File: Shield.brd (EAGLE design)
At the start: 53.3 x 55.9 mm, 26 parts, among them J1 AVR_SPI_PRG_6PTH, Q8 TIP120, U2 LM78XX-TO252-3, U4 ATMEGA328P_PDIP, Y1 16Mhz

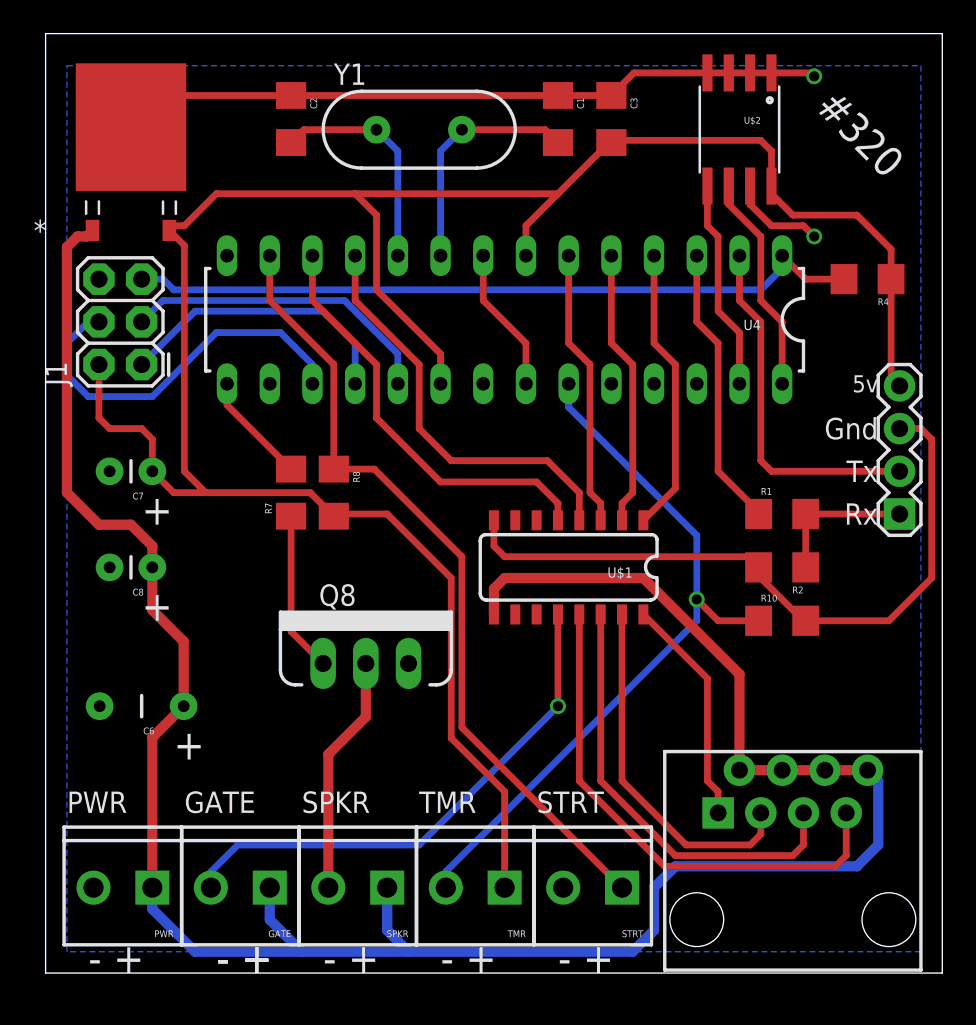
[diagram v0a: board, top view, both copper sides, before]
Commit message: Fixed 12v relay voltage
git-svn-id: svn+ssh://petrocik.net/home/svn/repo/uci_gate/branches/hardware/uci_gate/3.x@133 8c868176-b666-4d83-8e7f-acb7c29fc81a
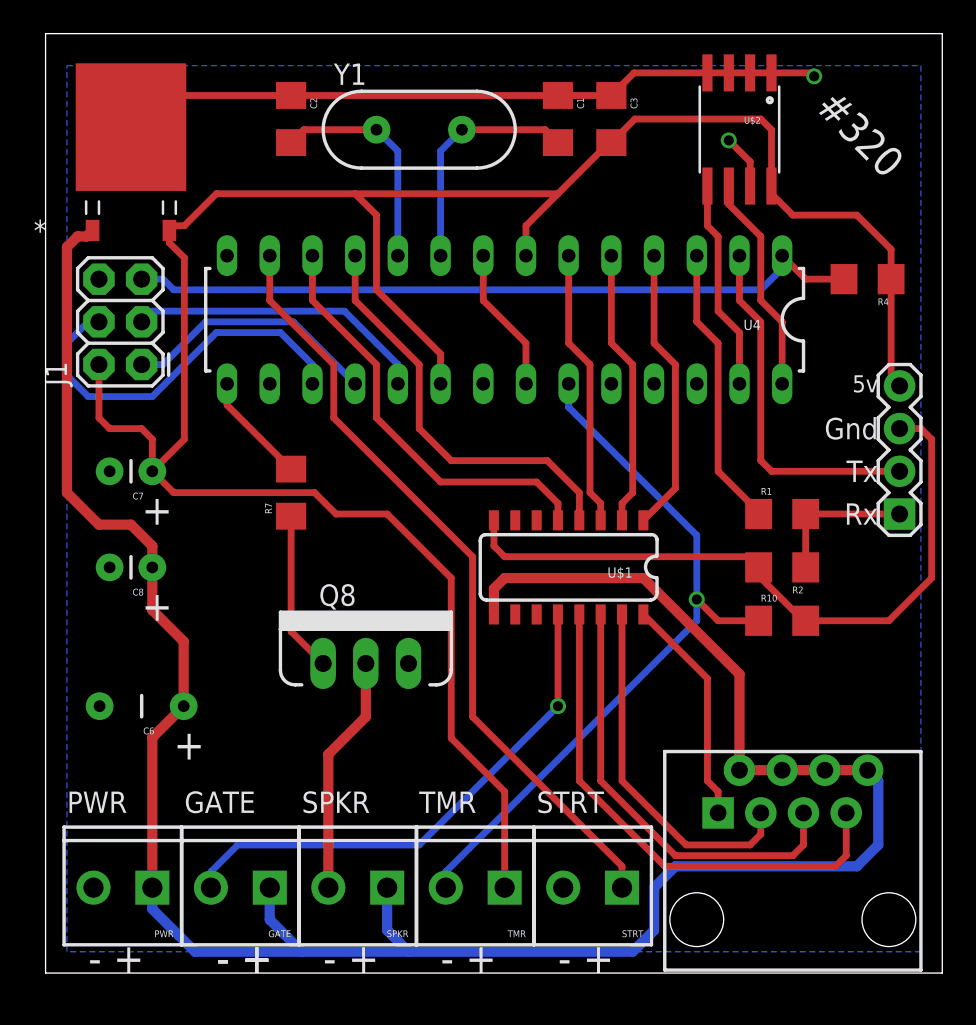
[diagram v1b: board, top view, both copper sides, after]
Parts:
- removed R8: 10K, SparkFun-Passives:1206
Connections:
- net 5V: no longer R8.2
- net D7: no longer R8.1
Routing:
- net GND: track 98.7 -> 96.3 mm
- net MISO: track 17.2 -> 15.3 mm
- net D7: track 47.7 -> 46.3 mm
- net SCK: track 18.9 -> 18.0 mm
- net 5V: track 141.1 -> 141.7 mm
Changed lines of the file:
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@@
 <?xml version="1.0" encoding="utf-8"?>
 <!DOCTYPE eagle SYSTEM "eagle.dtd">
-<eagle version="6.5.0">
+<eagle version="7.2.0">
 <drawing>
 <settings>
@@
 <pass name="Default">
 <param name="RoutingGrid" value="10mil"/>
+<param name="AutoGrid" value="1"/>
+<param name="Efforts" value="0"/>
+<param name="TopRouterVariant" value="1"/>
 <param name="tpViaShape" value="round"/>
 <param name="PrefDir.1" value="|"/>
@@
 <element name="SPKR" library="SparkFun-Connectors" package="SCREWTERMINAL-3.5MM-2" value="" x="20.32" y="5.08" rot="R180"/>
 <element name="Q8" library="ucigate" package="TO220V" value="TIP120" x="19.05" y="18.415"/>
-<element name="R8" library="SparkFun-Passives" package="1206" value="10K" x="17.145" y="28.575" rot="R270"/>
 <element name="STRT" library="SparkFun-Connectors" package="SCREWTERMINAL-3.5MM-2" value="" x="34.29" y="5.08" rot="R180"/>
 <element name="R10" library="SparkFun-Passives" package="1206" value="10K" x="43.815" y="20.955"/>
@@
 <wire x1="26.035" y1="40.005" x2="28.575" y2="37.465" width="0.4064" layer="1"/>
 <wire x1="28.575" y1="37.465" x2="28.575" y2="35.052" width="0.4064" layer="1"/>
-<polygon width="0.4064" layer="16">
+<polygon width="0.4064" layer="16" isolate="0.254">
 <vertex x="1.27" y="53.975"/>
 <vertex x="52.07" y="53.975"/>
@@
 <wire x1="50.8" y1="32.766" x2="50.8" y2="32.385" width="0.381" layer="1"/>
 <wire x1="43.18" y1="53.34" x2="43.18" y2="53.5432" width="0.381" layer="1"/>
-<via x="45.72" y="43.815" extent="1-16" drill="0.6"/>
-<wire x1="41.91" y1="46.8122" x2="41.91" y2="45.72" width="0.4064" layer="1"/>
-<wire x1="41.91" y1="45.72" x2="43.18" y2="44.45" width="0.4064" layer="1"/>
-<wire x1="43.18" y1="44.45" x2="45.085" y2="44.45" width="0.4064" layer="1"/>
-<wire x1="45.085" y1="44.45" x2="45.72" y2="43.815" width="0.4064" layer="1"/>
 <wire x1="45.215" y1="20.955" x2="45.085" y2="20.955" width="0.4064" layer="1"/>
 <wire x1="45.085" y1="20.955" x2="42.545" y2="23.495" width="0.4064" layer="1"/>
@@
 <wire x1="27.305" y1="24.765" x2="41.78" y2="24.765" width="0.4064" layer="1"/>
 <wire x1="41.78" y1="24.765" x2="42.415" y2="24.13" width="0.4064" layer="1"/>
+<wire x1="41.91" y1="46.8122" x2="41.91" y2="48.26" width="0.4064" layer="1"/>
+<wire x1="41.91" y1="48.26" x2="40.64" y2="49.53" width="0.4064" layer="1"/>
+<via x="40.64" y="49.53" extent="1-16" drill="0.6"/>
 </signal>
 <signal name="VCC">
@@
 </signal>
 <signal name="D7">
-<contactref element="R8" pad="1"/>
 <contactref element="STRT" pad="1"/>
 <contactref element="U4" pad="13"/>
+<wire x1="34.29" y1="5.08" x2="34.29" y2="6.35" width="0.4064" layer="1"/>
+<wire x1="34.29" y1="6.35" x2="25.4" y2="15.24" width="0.4064" layer="1"/>
+<wire x1="25.4" y1="15.24" x2="25.4" y2="24.765" width="0.4064" layer="1"/>
+<wire x1="25.4" y1="24.765" x2="17.145" y2="33.02" width="0.4064" layer="1"/>
 <wire x1="13.335" y1="42.672" x2="13.335" y2="40.005" width="0.4064" layer="1"/>
 <wire x1="13.335" y1="40.005" x2="17.145" y2="36.195" width="0.4064" layer="1"/>
-<wire x1="17.145" y1="36.195" x2="17.145" y2="29.975" width="0.4064" layer="1"/>
-<wire x1="17.145" y1="29.975" x2="19.555" y2="29.975" width="0.4064" layer="1"/>
-<wire x1="19.555" y1="29.975" x2="24.765" y2="24.765" width="0.4064" layer="1"/>
-<wire x1="24.765" y1="24.765" x2="24.765" y2="14.605" width="0.4064" layer="1"/>
-<wire x1="24.765" y1="14.605" x2="34.29" y2="5.08" width="0.4064" layer="1"/>
+<wire x1="17.145" y1="36.195" x2="17.145" y2="33.02" width="0.4064" layer="1"/>
 </signal>
 <signal name="A0">
@@
 <contactref element="BT_HDR" pad="4"/>
 <contactref element="U$2" pad="8"/>
-<contactref element="R8" pad="2"/>
 <contactref element="C7" pad="1"/>
 <contactref element="J1" pad="2"/>
@@
 <wire x1="44.45" y1="45.085" x2="43.18" y2="46.355" width="0.4064" layer="1"/>
 <wire x1="43.18" y1="46.355" x2="43.18" y2="46.8122" width="0.4064" layer="1"/>
-<wire x1="43.18" y1="46.8122" x2="43.18" y2="48.895" width="0.4064" layer="1"/>
-<wire x1="43.18" y1="48.895" x2="42.545" y2="49.53" width="0.4064" layer="1"/>
-<wire x1="42.545" y1="49.53" x2="33.785" y2="49.53" width="0.4064" layer="1"/>
-<wire x1="33.785" y1="49.53" x2="33.655" y2="49.4" width="0.4064" layer="1"/>
 <wire x1="33.655" y1="49.4" x2="33.525" y2="49.4" width="0.4064" layer="1"/>
 <wire x1="33.525" y1="49.4" x2="30.48" y2="46.355" width="0.4064" layer="1"/>
@@
 <wire x1="24.13" y1="23.495" x2="20.32" y2="27.305" width="0.4064" layer="1"/>
 <wire x1="20.32" y1="27.305" x2="17.275" y2="27.305" width="0.4064" layer="1"/>
-<wire x1="17.275" y1="27.305" x2="17.145" y2="27.175" width="0.4064" layer="1"/>
-<wire x1="7.62" y1="28.575" x2="9.525" y2="28.575" width="0.4064" layer="1"/>
-<wire x1="9.525" y1="28.575" x2="15.745" y2="28.575" width="0.4064" layer="1"/>
-<wire x1="15.745" y1="28.575" x2="17.145" y2="27.175" width="0.4064" layer="1"/>
+<wire x1="7.62" y1="28.575" x2="16.005" y2="28.575" width="0.4064" layer="1"/>
 <wire x1="6.35" y1="29.845" x2="7.62" y2="28.575" width="0.4064" layer="1"/>
 <wire x1="6.35" y1="29.845" x2="6.35" y2="31.75" width="0.4064" layer="1"/>
@@
 <wire x1="3.81" y1="32.385" x2="3.175" y2="33.02" width="0.4064" layer="1"/>
 <wire x1="3.175" y1="33.02" x2="3.175" y2="36.195" width="0.4064" layer="1"/>
-<wire x1="7.366" y1="44.1706" x2="8.255" y2="43.2816" width="0.4064" layer="1"/>
-<wire x1="8.255" y1="43.2816" x2="8.255" y2="29.845" width="0.4064" layer="1"/>
-<wire x1="8.255" y1="29.845" x2="9.525" y2="28.575" width="0.4064" layer="1"/>
+<wire x1="43.18" y1="46.8122" x2="43.18" y2="50.165" width="0.4064" layer="1"/>
+<wire x1="43.18" y1="50.165" x2="42.545" y2="50.8" width="0.4064" layer="1"/>
+<wire x1="42.545" y1="50.8" x2="35.055" y2="50.8" width="0.4064" layer="1"/>
+<wire x1="35.055" y1="50.8" x2="33.655" y2="49.4" width="0.4064" layer="1"/>
+<wire x1="17.275" y1="27.305" x2="16.005" y2="28.575" width="0.4064" layer="1"/>
+<wire x1="7.366" y1="44.1706" x2="7.366" y2="43.434" width="0.4064" layer="1"/>
+<wire x1="7.366" y1="43.434" x2="8.255" y2="42.545" width="0.4064" layer="1"/>
+<wire x1="8.255" y1="42.545" x2="8.255" y2="31.75" width="0.4064" layer="1"/>
+<wire x1="8.255" y1="31.75" x2="6.35" y2="29.845" width="0.4064" layer="1"/>
 </signal>
 <signal name="D2">
@@
 <contactref element="J1" pad="1"/>
 <contactref element="U4" pad="18"/>
-<wire x1="5.715" y1="36.195" x2="8.89" y2="39.37" width="0.4064" layer="16"/>
-<wire x1="8.89" y1="39.37" x2="16.51" y2="39.37" width="0.4064" layer="16"/>
-<wire x1="16.51" y1="39.37" x2="18.415" y2="37.465" width="0.4064" layer="16"/>
-<wire x1="18.415" y1="37.465" x2="18.415" y2="35.052" width="0.4064" layer="16"/>
+<wire x1="5.715" y1="36.195" x2="6.985" y2="36.195" width="0.4064" layer="16"/>
+<wire x1="6.985" y1="36.195" x2="9.525" y2="38.735" width="0.4064" layer="16"/>
+<wire x1="9.525" y1="38.735" x2="14.732" y2="38.735" width="0.4064" layer="16"/>
+<wire x1="14.732" y1="38.735" x2="18.415" y2="35.052" width="0.4064" layer="16"/>
 </signal>
 <signal name="SCK">
 <contactref element="J1" pad="3"/>
 <contactref element="U4" pad="19"/>
-<wire x1="20.955" y1="35.052" x2="20.955" y2="36.83" width="0.4064" layer="16"/>
-<wire x1="20.955" y1="36.83" x2="17.78" y2="40.005" width="0.4064" layer="16"/>
-<wire x1="17.78" y1="40.005" x2="6.985" y2="40.005" width="0.4064" layer="16"/>
-<wire x1="6.985" y1="40.005" x2="5.715" y2="38.735" width="0.4064" layer="16"/>
+<wire x1="6.35" y1="39.37" x2="17.78" y2="39.37" width="0.4064" layer="16"/>
+<wire x1="17.78" y1="39.37" x2="20.955" y2="36.195" width="0.4064" layer="16"/>
+<wire x1="20.955" y1="36.195" x2="20.955" y2="35.052" width="0.4064" layer="16"/>
+<wire x1="6.35" y1="39.37" x2="5.715" y2="38.735" width="0.4064" layer="16"/>
 </signal>
 <signal name="MOSI">
@@
 <wire x1="6.985" y1="41.275" x2="7.62" y2="40.64" width="0.4064" layer="16"/>
 <wire x1="7.62" y1="40.64" x2="42.545" y2="40.64" width="0.4064" layer="16"/>
-<wire x1="42.545" y1="40.64" x2="44.196" y2="42.291" width="0.4064" layer="16"/>
 <wire x1="44.196" y1="42.291" x2="43.815" y2="42.672" width="0.4064" layer="16"/>
+<wire x1="42.545" y1="40.64" x2="43.815" y2="41.91" width="0.4064" layer="16"/>
+<wire x1="43.815" y1="41.91" x2="43.815" y2="42.672" width="0.4064" layer="16"/>
 </signal>
 <signal name="D6">
